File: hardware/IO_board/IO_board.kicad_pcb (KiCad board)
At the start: 2 copper layers, 26.8 x 25.8 mm, 8 parts, among them J1 DF12NB(3.0)-30DS-0.5V(51), J3 Conn_01x31, J4 DF12NB(3.0)-30DS-0.5V(51), J5 Conn_01x31, J6 Conn_01x06, J7 Combined I/O

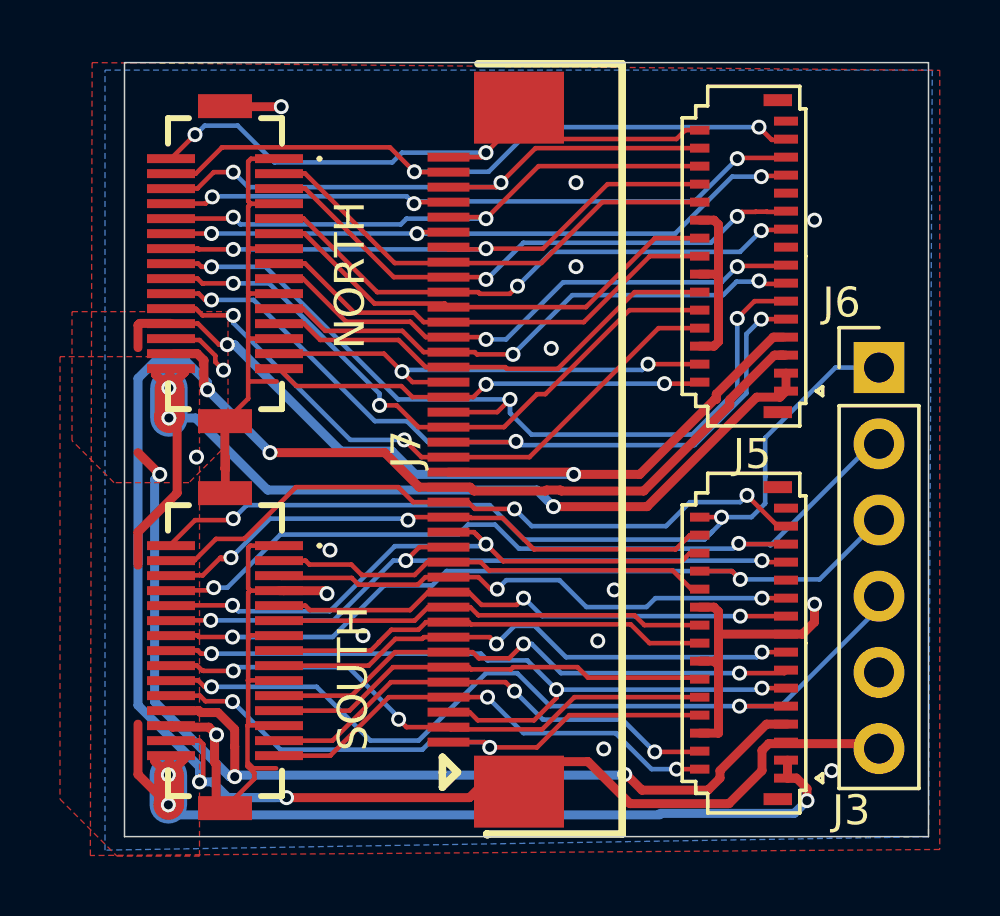
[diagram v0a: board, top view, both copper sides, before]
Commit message: fixed mixup of pins G5/G4 (3rd diff pair ODD) and DE/PCLK (3rd diff pair EVEN), now with correct polarity for diff pairs
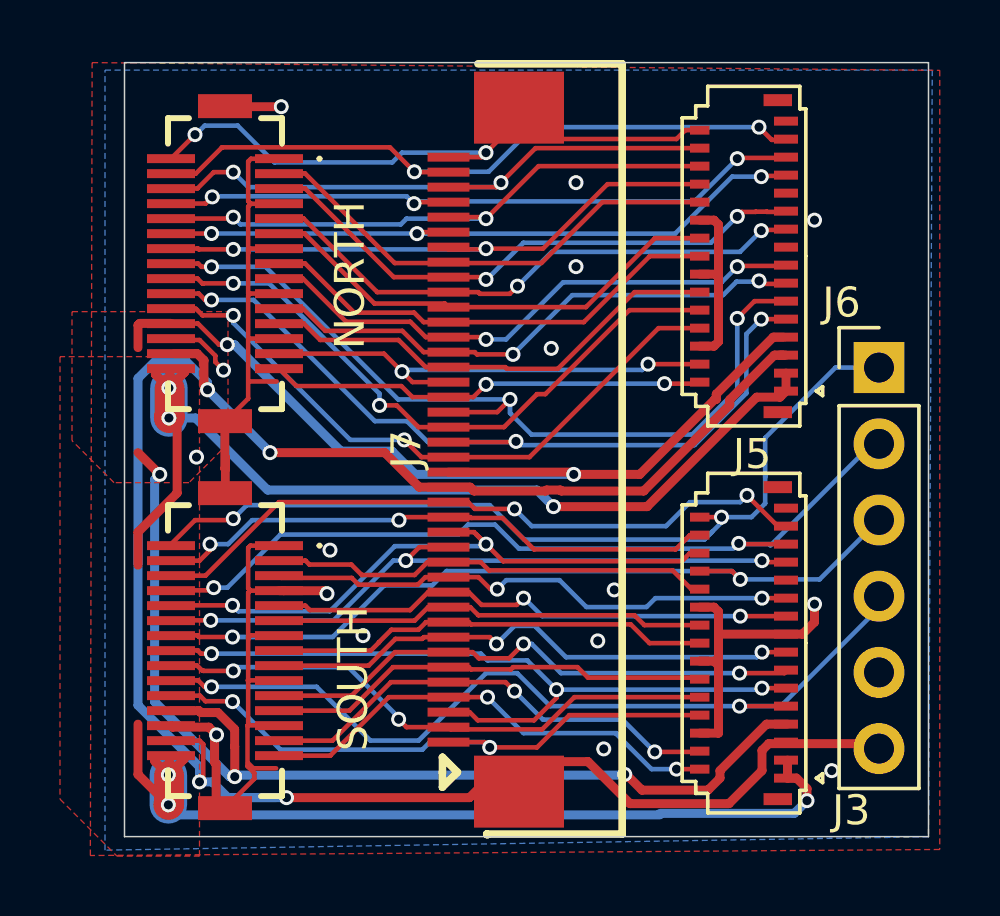
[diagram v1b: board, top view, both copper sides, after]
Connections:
- J4 pad 4: /G4 -> /G5
- J4 pad 6: /G5 -> /G4
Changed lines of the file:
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@@
 			(size 0.3 1.6)
 			(layers "F.Cu" "F.Paste" "F.Mask")
-			(net 26 "/G4")
+			(net 31 "/G5")
 			(pinfunction "3")
 			(pintype "passive")
@@
 			(size 0.3 1.6)
 			(layers "F.Cu" "F.Paste" "F.Mask")
-			(net 31 "/G5")
+			(net 26 "/G4")
 			(pinfunction "5")
 			(pintype "passive")
@@
 	)
 	(segment
-		(start 130.484166 92.590834)
-		(end 129.661838 92.590834)
+		(start 139.827 90.875)
+		(end 139.602 90.65)
 		(width 0.154)
 		(layer "F.Cu")
@@
 	)
 	(segment
-		(start 131.2 91.875)
-		(end 130.484166 92.590834)
+		(start 133.3 90.65)
+		(end 130.85 93.1)
 		(width 0.154)
 		(layer "F.Cu")
@@
 	)
 	(segment
-		(start 137.275 90.15)
-		(end 133.866079 90.15)
-		(width 0.154)
-		(layer "F.Cu")
-		(net 26)
-	)
-	(segment
-		(start 137.775 90.65)
-		(end 137.275 90.15)
-		(width 0.154)
-		(layer "F.Cu")
-		(net 26)
-	)
-	(segment
-		(start 133.866079 90.15)
-		(end 132.141079 91.875)
+		(start 139.602 90.65)
+		(end 133.3 90.65)
 		(width 0.154)
 		(layer "F.Cu")
@@
 	)
 	(segment
-		(start 139.602 90.65)
-		(end 137.775 90.65)
+		(start 130.85 93.1)
+		(end 129.7 93.1)
 		(width 0.154)
 		(layer "F.Cu")
@@
 		(net 26)
 	)
-	(segment
-		(start 139.827 90.875)
-		(end 139.602 90.65)
-		(width 0.154)
-		(layer "F.Cu")
-		(net 26)
-	)
-	(segment
-		(start 132.141079 91.875)
-		(end 131.2 91.875)
-		(width 0.154)
-		(layer "F.Cu")
-		(net 26)
-	)
 	(via
 		(at 148.9 90.425)
@@
 	)
 	(segment
-		(start 146.996 91.75)
-		(end 147.35 91.75)
-		(width 0.154)
-		(layer "F.Cu")
-		(net 31)
-	)
-	(segment
-		(start 131.7 92.5)
-		(end 131.65 92.55)
+		(start 139.701079 91.179)
+		(end 140.754 91.179)
 		(width 0.154)
 		(layer "F.Cu")
@@
 	)
 	(segment
-		(start 137.7 91.15)
-		(end 139.672079 91.15)
+		(start 139.672079 91.15)
+		(end 139.701079 91.179)
 		(width 0.154)
 		(layer "F.Cu")
@@
 	)
 	(segment
-		(start 140.754 91.179)
-		(end 141.8 92.225)
+		(start 131 92.05)
+		(end 131 92.254)
 		(width 0.154)
 		(layer "F.Cu")
@@
 	)
 	(segment
-		(start 131.35 92.5)
-		(end 130.759166 93.090834)
+		(start 131 92.254)
+		(end 130.654 92.6)
 		(width 0.154)
 		(layer "F.Cu")
@@
 	)
 	(segment
-		(start 141.8 92.225)
-		(end 146.521 92.225)
+		(start 130.654 92.6)
+		(end 129.7 92.6)
 		(width 0.154)
 		(layer "F.Cu")
@@
 	)
 	(segment
-		(start 139.672079 91.15)
-		(end 139.701079 91.179)
+		(start 131 92.05)
+		(end 131.15 92.05)
 		(width 0.154)
 		(layer "F.Cu")
@@
 	)
 	(segment
-		(start 131.7 92.5)
-		(end 131.35 92.5)
+		(start 137.4 91.15)
+		(end 139.672079 91.15)
 		(width 0.154)
 		(layer "F.Cu")
@@
 	)
 	(segment
-		(start 131.65 92.55)
-		(end 131.37992 92.55)
+		(start 146.521 92.225)
+		(end 146.996 91.75)
 		(width 0.154)
 		(layer "F.Cu")
@@
 	)
 	(segment
-		(start 130.759166 93.090834)
-		(end 129.661838 93.090834)
+		(start 141.8 92.225)
+		(end 146.521 92.225)
 		(width 0.154)
 		(layer "F.Cu")
@@
 	)
 	(segment
-		(start 146.521 92.225)
-		(end 146.996 91.75)
+		(start 140.754 91.179)
+		(end 141.8 92.225)
 		(width 0.154)
 		(layer "F.Cu")
@@
 	)
 	(segment
-		(start 137.6 91.25)
-		(end 137.7 91.15)
+		(start 137.3 91.25)
+		(end 137.4 91.15)
 		(width 0.154)
 		(layer "F.Cu")
@@
 	)
 	(segment
-		(start 139.701079 91.179)
-		(end 140.754 91.179)
+		(start 146.996 91.75)
+		(end 147.35 91.75)
 		(width 0.154)
 		(layer "F.Cu")
@@
 	)
 	(via
-		(at 137.6 91.25)
+		(at 137.3 91.25)
 		(size 0.5)
 		(drill 0.3)
@@
 	)
 	(via
-		(at 131.7 92.5)
+		(at 131 92.05)
 		(size 0.5)
 		(drill 0.3)
@@
 	)
 	(segment
-		(start 133 91.2)
-		(end 137.55 91.2)
+		(start 131.605237 92.05)
+		(end 131 92.05)
 		(width 0.154)
 		(layer "B.Cu")
@@
 	)
 	(segment
-		(start 131.7 92.5)
-		(end 133 91.2)
+		(start 132.405237 91.25)
+		(end 131.605237 92.05)
 		(width 0.154)
 		(layer "B.Cu")
@@
 	)
 	(segment
-		(start 137.55 91.2)
-		(end 137.6 91.25)
+		(start 137.3 91.25)
+		(end 132.405237 91.25)
 		(width 0.154)
 		(layer "B.Cu")
